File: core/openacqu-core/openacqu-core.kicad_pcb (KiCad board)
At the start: 2 copper layers, 45 x 36 mm, 33 parts, among them J1 GSB1C41110SSHR, U1 QFN65P400X400X10-17N, U2 LP5817DRLR, U3 FXL6408UMX, U4 24AA025E48T-E_OT, U5 AP2112K-3.3TRG1, U6 TPS22996HQDYCRQ1

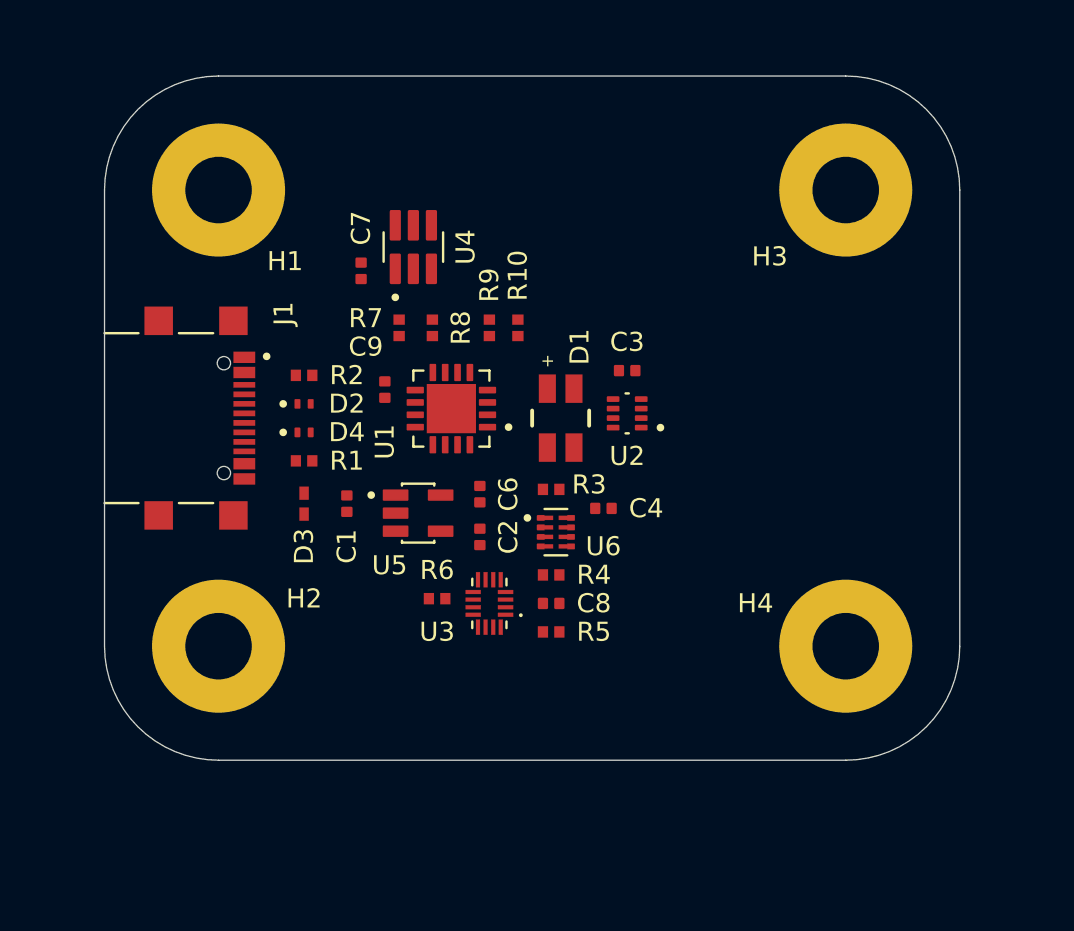
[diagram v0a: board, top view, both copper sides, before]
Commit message: Routed core design
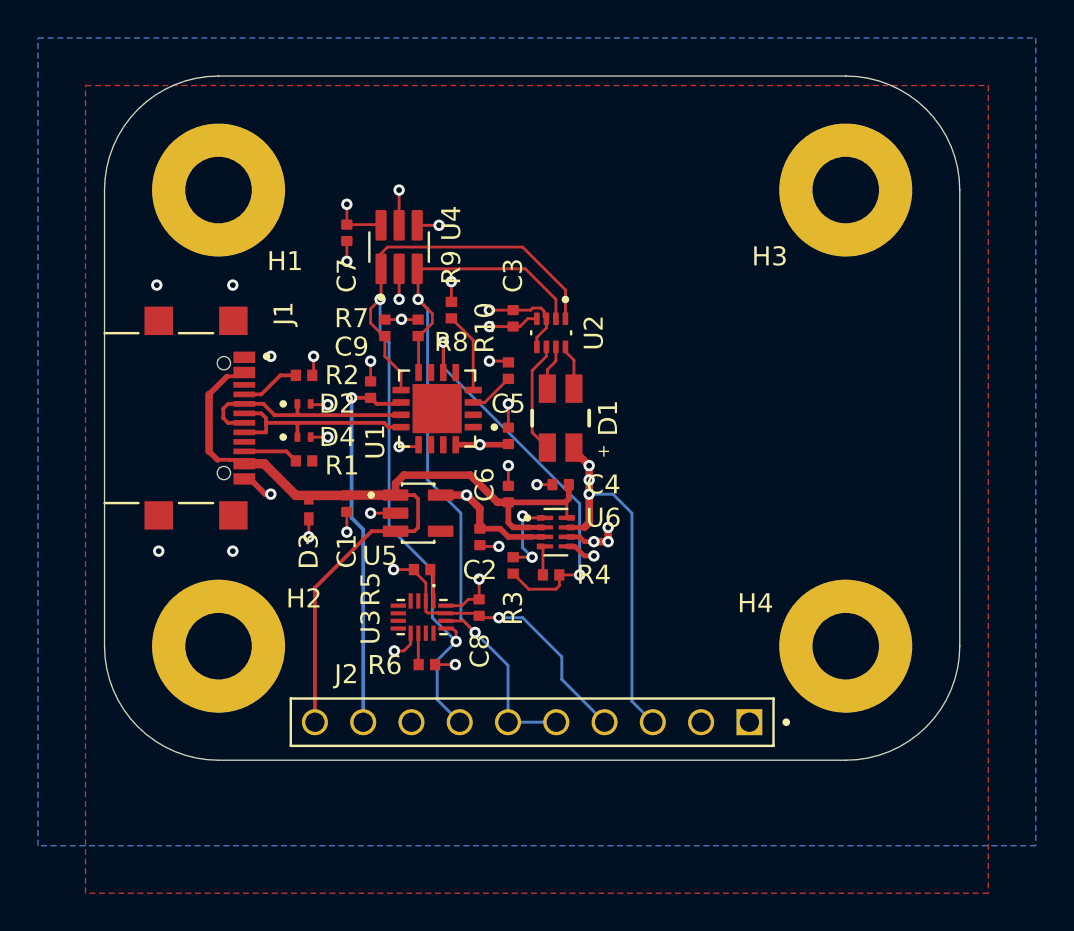
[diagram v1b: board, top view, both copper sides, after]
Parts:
- added C5: 1uF, openacqu_footprints:CAPC1005X55N, F.Cu at (92.2, 75.9)
- added J2: Test Points, openacqu_footprints:MLE_TSHC-110-S-14-295-G-LF, F.Cu at (93.5, 91.0)
- U1: value QFN65P400X400X10-17N -> MCP2221AT-I_ML
- moved R5 7.54 mm to (87.7, 83.0), turned to 0 degrees
- moved C3 6.60 mm to (92.5, 69.8), turned to 90 degrees
- moved U2 5.83 mm to (94.5, 70.5), turned to -90 degrees
- moved R3 4.47 mm to (92.5, 82.8), turned to 90 degrees
- moved C8 3.80 mm to (90.7, 85.0), turned to 90 degrees
- moved U3 3.61 mm to (87.7, 85.5), turned to -90 degrees
- moved R6 3.51 mm to (88.0, 88.0), turned to 180 degrees
- moved C4 2.57 mm to (95.0, 78.5), turned to 180 degrees
- moved R10 2.30 mm to (92.2, 72.5)
- moved R9 2.21 mm to (89.2, 69.3)
- moved C7 2.14 mm to (83.8, 65.2)
- moved C6 1.50 mm to (92.2, 79.0)
- moved C9 0.75 mm to (85.0, 73.5)
- moved R7 0.75 mm to (85.8, 70.2)
- moved R8 0.75 mm to (87.5, 70.2)
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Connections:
- U2 pad 7: /LED_R -> /LED_G
- U2 pad 8: /LED_G -> /LED_R
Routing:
- net VBUS: track 0.00 -> 50.0 mm
- net /SCL: track 0.00 -> 46.3 mm, vias 0 -> 2
- net /SDA: track 0.00 -> 43.7 mm, vias 0 -> 2
- net GND: track 0.00 -> 32.0 mm, vias 0 -> 27
- net +3V3: track 0.00 -> 30.9 mm, vias 0 -> 4
- net +3V3_SYS: track 0.00 -> 27.6 mm, vias 0 -> 9
- net /USBCFG: track 0.00 -> 21.3 mm, vias 0 -> 2
- net +5V0_SYS: track 0.00 -> 19.7 mm, vias 0 -> 3
- net /DN: track 0.00 -> 12.1 mm
- net /DP: track 0.00 -> 10.9 mm
- net /LED_B: track 0.00 -> 6.24 mm
- net /ON1: track 0.00 -> 4.59 mm, vias 0 -> 2
- net /MCP_URX: track 0.00 -> 4.39 mm
- net /CC1: track 0.00 -> 3.13 mm
- net /CC2: track 0.00 -> 2.92 mm
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- added copper zone on In2.Cu, net +3V3
- added copper zone on In2.Cu, net +3V3_SYS
- added copper zone on B.Cu, net GND
- added copper zone on F.Cu, net GND
- added copper zone on In1.Cu, net GND
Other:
- copper layers 2 -> 4

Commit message: Moved core to separate sheet
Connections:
- net /CC1 renamed /Core/CC1
- net /CC2 renamed /Core/CC2
- net /DN renamed /Core/DN
- net /DP renamed /Core/DP
- net /FX_INT renamed /Core/FX_INT
- net /FX_RST renamed /Core/FX_RST
- net /LED_B renamed /Core/LED_B
- net /LED_G renamed /Core/LED_G
- net /LED_R renamed /Core/LED_R
- net /MCP_RST renamed /Core/MCP_RST
- net /MCP_URX renamed /Core/MCP_URX
- net /ON1 renamed /Core/ON1
- net /ON2 renamed /Core/ON2
- net /SCL renamed /Core/SCL
- net /SDA renamed /Core/SDA
- net /USBCFG renamed /Core/USBCFG
